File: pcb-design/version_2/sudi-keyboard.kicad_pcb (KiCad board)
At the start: 2 copper layers, 123.4 x 99.4 mm, 170 parts, among them J1 SIDE_CON, J2 SWD_JLINK, J3 0.91 OLED, J4 BatCon, J5 SIDE_CON, K1 KEYSW, K10 KEYSW, K11 KEYSW, K12 KEYSW, K13 KEYSW, K14 KEYSW, K15 KEYSW, K16 KEYSW, K17 KEYSW, K18 KEYSW, K2 KEYSW, K3 KEYSW, K4 KEYSW, K5 KEYSW, K6 KEYSW, K7 KEYSW, K8 KEYSW, K9 KEYSW, P1 USB_C_Plug_USB2.0, Q1 PJA3404_(G1,D3,S2), Q2 PJA3405_(G1,D3,S2), SW1 RST, SW3 PWR_SWITCH, SW4 5V_EN, U10 MAX17048, U4 CH340C, U5 BQ24075RGT_DPPM, U6 TPS63002_SEPIC_5V, U7 nRF52832-QFxx, U8 MCP23017_SS, U9 TPS63001_SEPIC_3V3, Y1 32MHz_CF4032M00020001

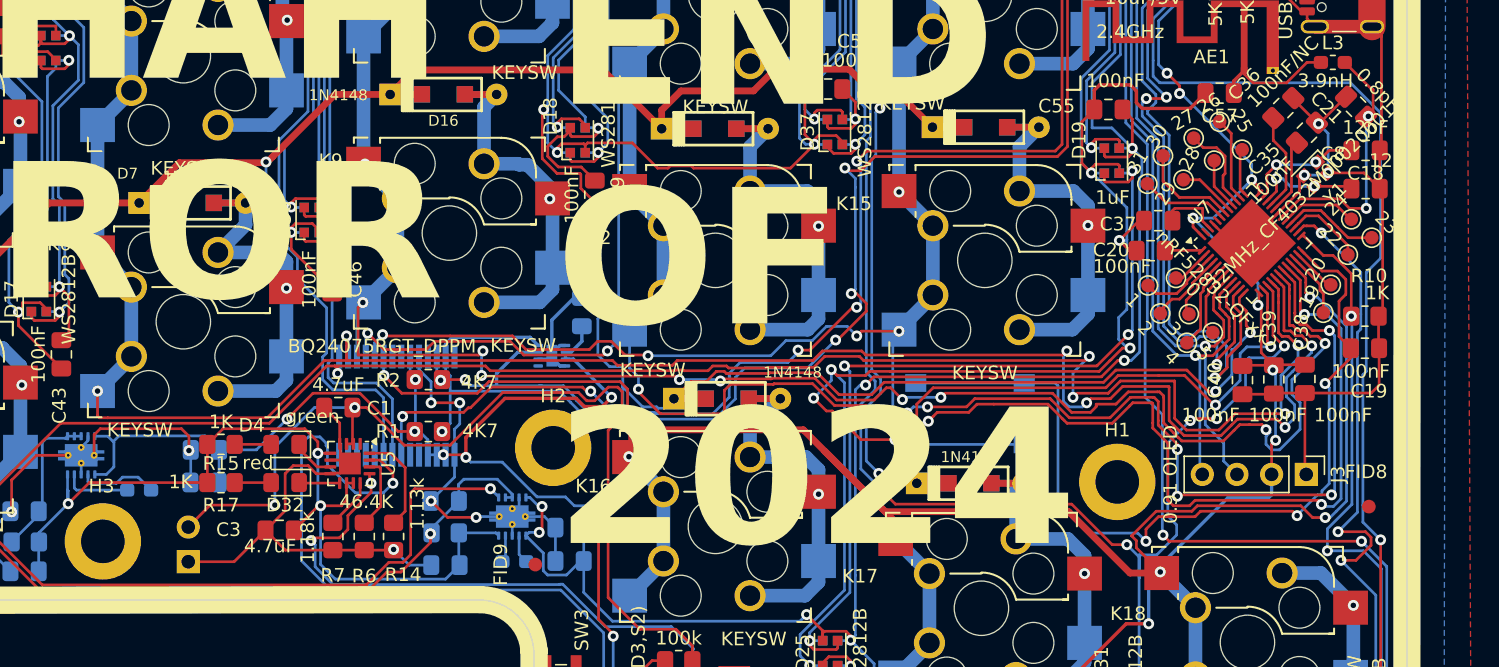
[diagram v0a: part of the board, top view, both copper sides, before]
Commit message: feat(component): change component to correct size
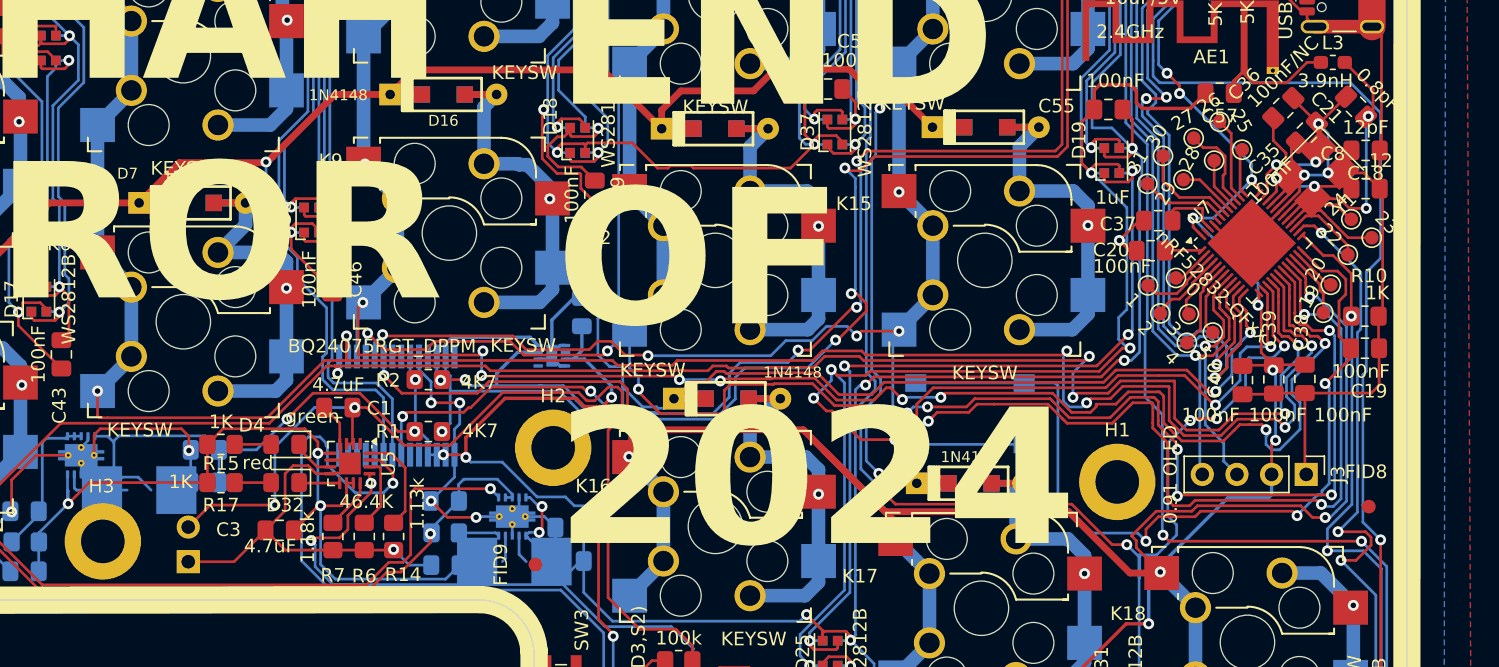
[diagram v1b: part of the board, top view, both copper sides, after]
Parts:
- L1, L2: footprint Inductor_SMD:L_0603_1608Metric_Pad1.05x0.95mm_HandSolder -> Inductor_SMD:L_Bourns_SRP7028A_7.3x6.6mm
- Y1: footprint Crystal:Crystal_SMD_2016-4Pin_2.0x1.6mm -> Crystal:Crystal_SMD_3225-4Pin_3.2x2.5mm_HandSoldering
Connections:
- U10 pad 2: +3.3V -> +BATT
